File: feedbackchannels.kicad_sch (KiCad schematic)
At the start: 81 parts, among them J18 FB CH1, J19 FB CH2, J20 FB CH3, J21 FB CH4, J22 VDET CH1, J23 VDET CH2, U21 TLP2366, U22 TLP2366, U23 TLP2366, U24 TLP2366, U25 TLP2366, U26 TLP2366, U27 TLV7031, U28 TLV7031, U29 TLP2366, U30 TLP2366, U31 74LVC1G126, U32 PCA9534, U33 SN74LVC541A

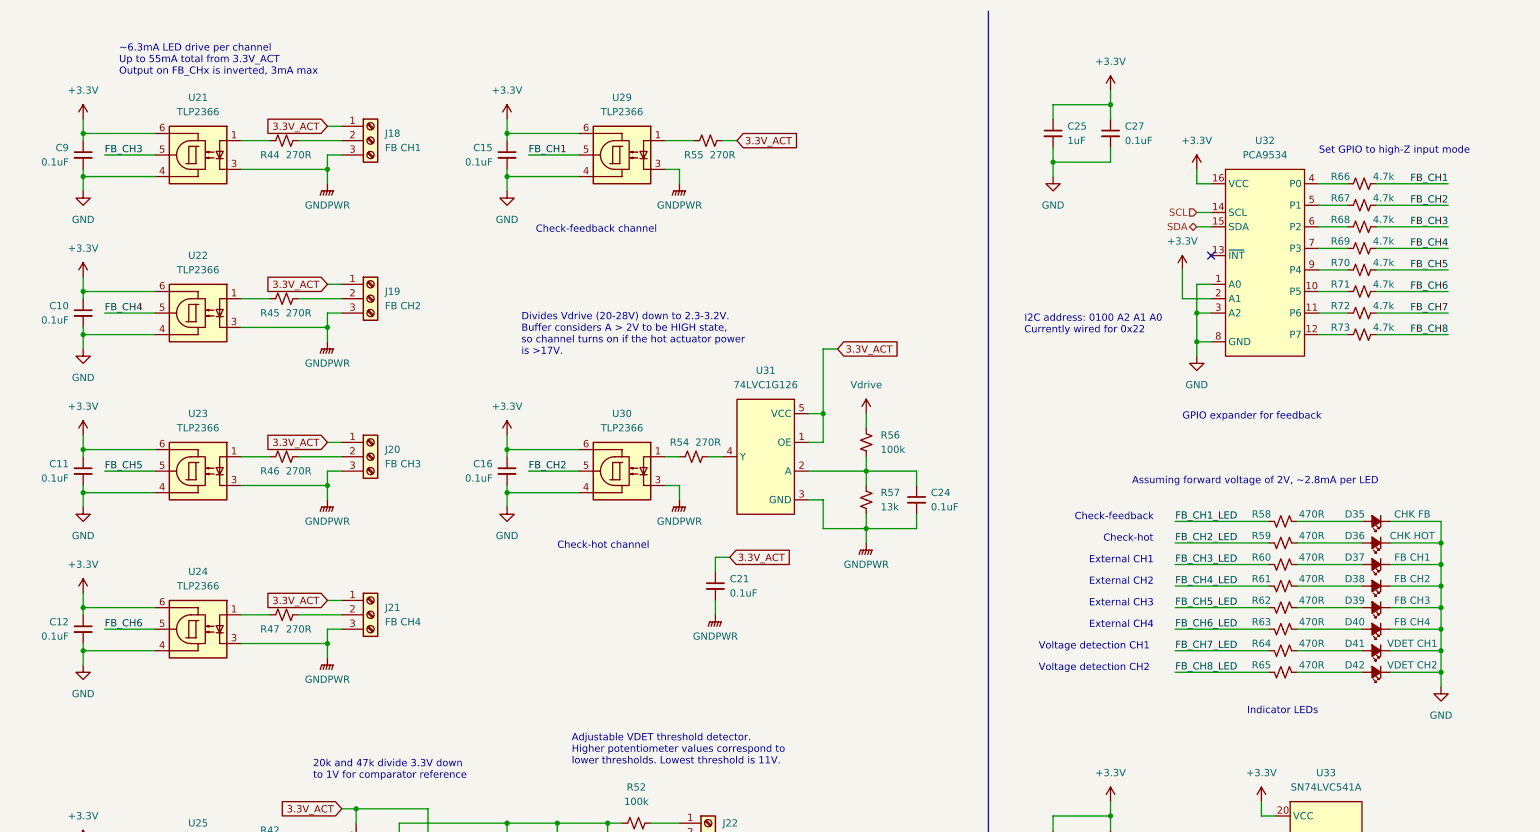
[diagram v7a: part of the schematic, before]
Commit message: Check-safe channel, footprint changes
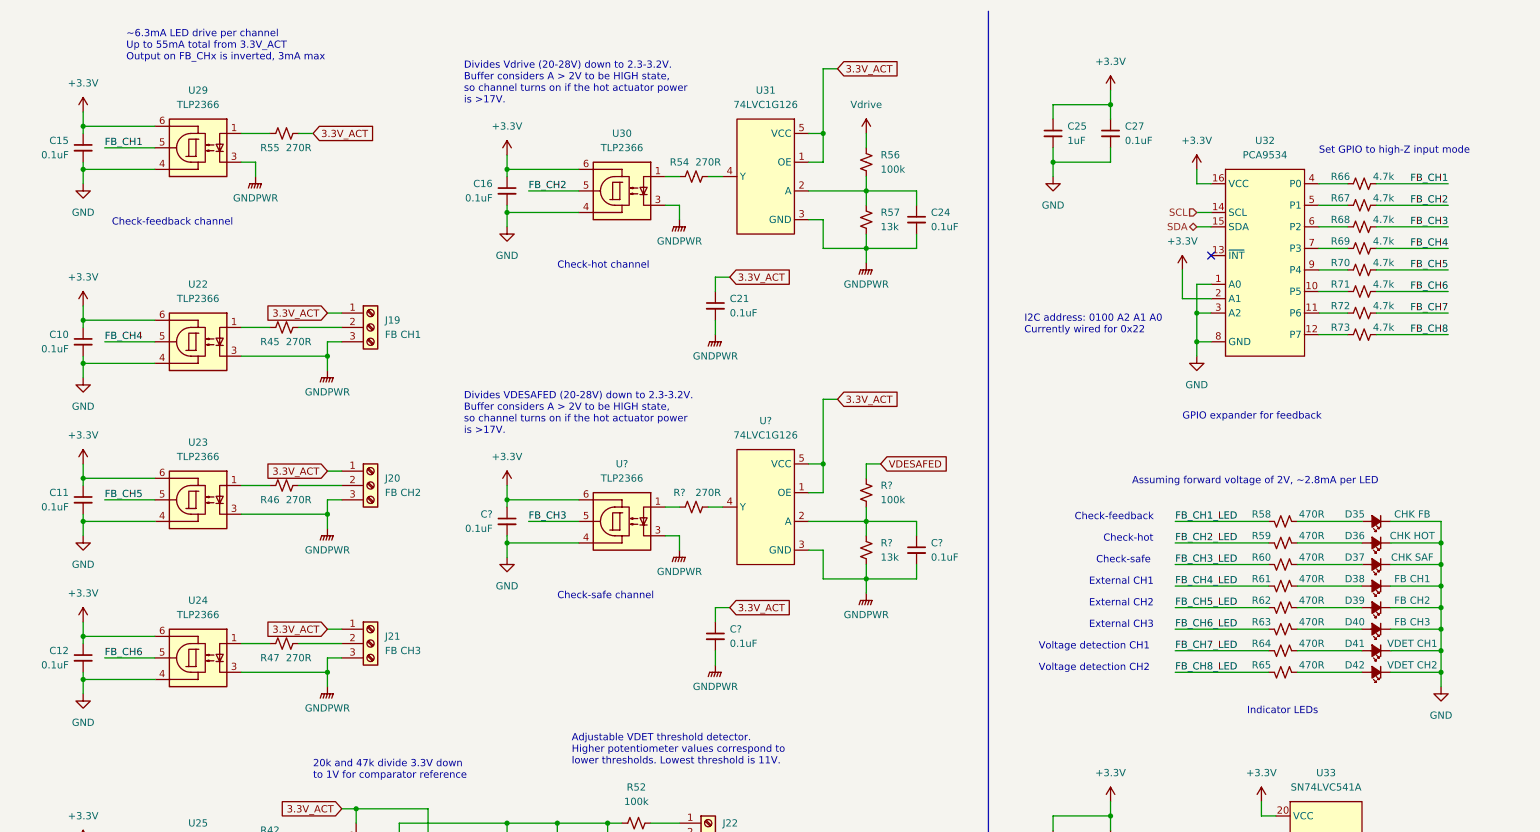
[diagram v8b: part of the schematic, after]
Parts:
- removed C9: 0.1uF, Capacitor_SMD:C_0603_1608Metric, symbol Device:C_Small
- removed J18: FB CH1, actuation:1751251, symbol Connector:Screw_Terminal_01x03
- removed R44: 270R, Resistor_SMD:R_0603_1608Metric, symbol Device:R_Small_US
- removed U21: TLP2366, actuation:TLP2366, symbol actuation:TLP2366
- added C? (x3): 0.1uF, Capacitor_SMD:C_0603_1608Metric, symbol Device:C_Small
- added R?: 270R, Resistor_SMD:R_0603_1608Metric, symbol Device:R_Small_US
- added R?: 100k, Resistor_SMD:R_0603_1608Metric, symbol Device:R_Small_US
- added R?: 13k, Resistor_SMD:R_0603_1608Metric, symbol Device:R_Small_US
- added U?: TLP2366, actuation:TLP2366, symbol actuation:TLP2366
- added U?: 74LVC1G126, Package_TO_SOT_SMD:SOT-23-5, symbol actuation:74LVC1G126
- D37: value FB CH1 -> CHK SAF
- D38: value FB CH2 -> FB CH1
- D39: value FB CH3 -> FB CH2
- D40: value FB CH4 -> FB CH3
- J19: value FB CH2 -> FB CH1; footprint actuation:1751251 -> (none); MPN 1751251 -> 1935174
- J20: value FB CH3 -> FB CH2; footprint actuation:1751251 -> (none); MPN 1751251 -> 1935174
- J21: value FB CH4 -> FB CH3; footprint actuation:1751251 -> (none); MPN 1751251 -> 1935174
- J22, J23: footprint actuation:1751248 -> (none); MPN 1751248 -> 1935161
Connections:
- net +3.3V: now also C?.1, U?.6
- net 3.3V_ACT: now also C?.1, U?.1 (OE), U?.5 (VCC)
- net FB_CH3: now also U?.5
- net GND: now also C?.2, U?.4
- net GNDPWR: now also C?.2, C?.2, R?.2, U?.3, U?.3 (GND)
- new net: R?.2, U?.1
- new net: R?.1, U?.4 (Y)
- new net: C?.1, R?.1, R?.2, U?.2 (A)
- new net VDESAFED: R?.1
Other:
- note added: "Check-safe"
- note added: "Check-safe channel"
- note added: "Divides VDESAFED (20-28V) down to 2.3-3.2V. Buffer considers A > 2V to be HIGH state, so channel turns on if the hot actuator power is >17V."
- note removed: "External CH4"
- moved on the sheet: C10, C11, C12, C15, C16, C21, C24, J19, J20, J21, R45, R46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
